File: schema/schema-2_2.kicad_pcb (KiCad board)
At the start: 2 copper layers, 91.4 x 55.9 mm, 16 parts, among them J1 Conn_01x04_Male, J2 Conn_01x04_Male, J3 Conn_01x05_Male

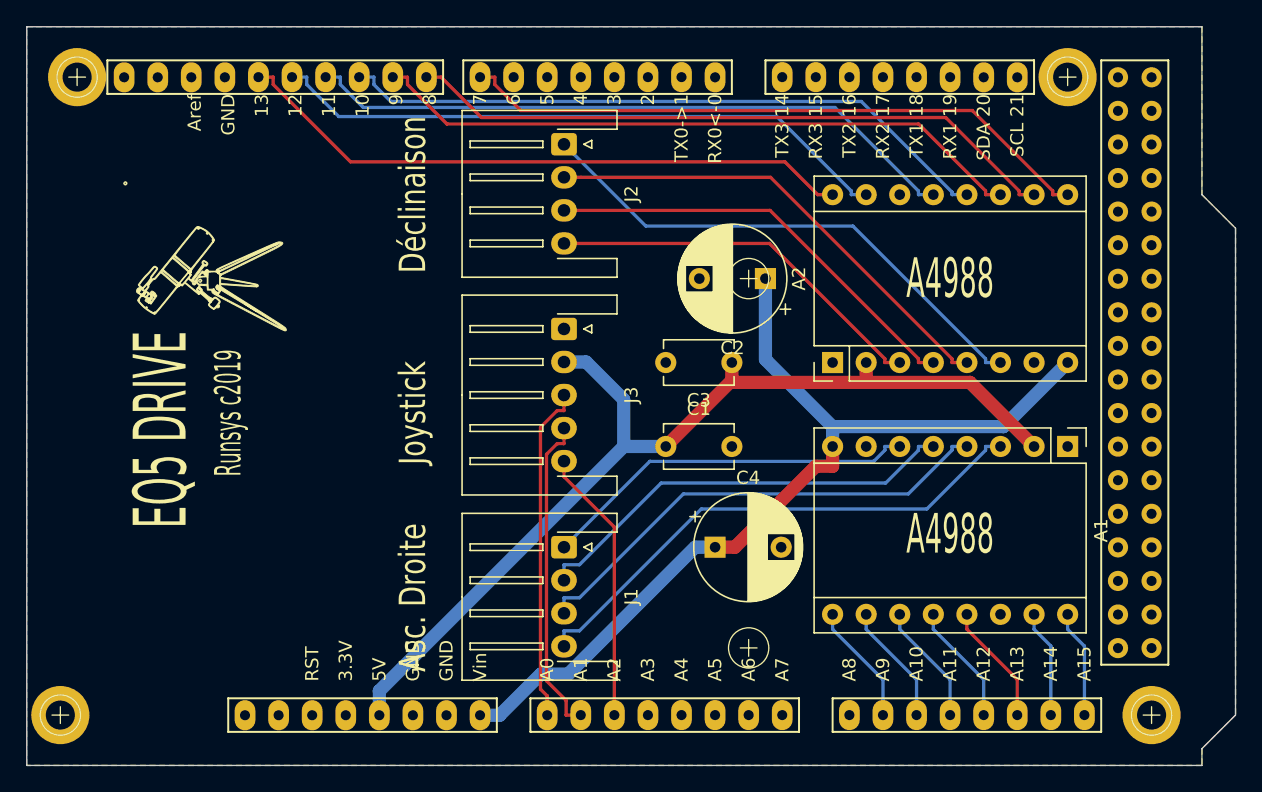
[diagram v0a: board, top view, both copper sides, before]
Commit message: Changement des noms de version Ajout de la macro python freeroute.py
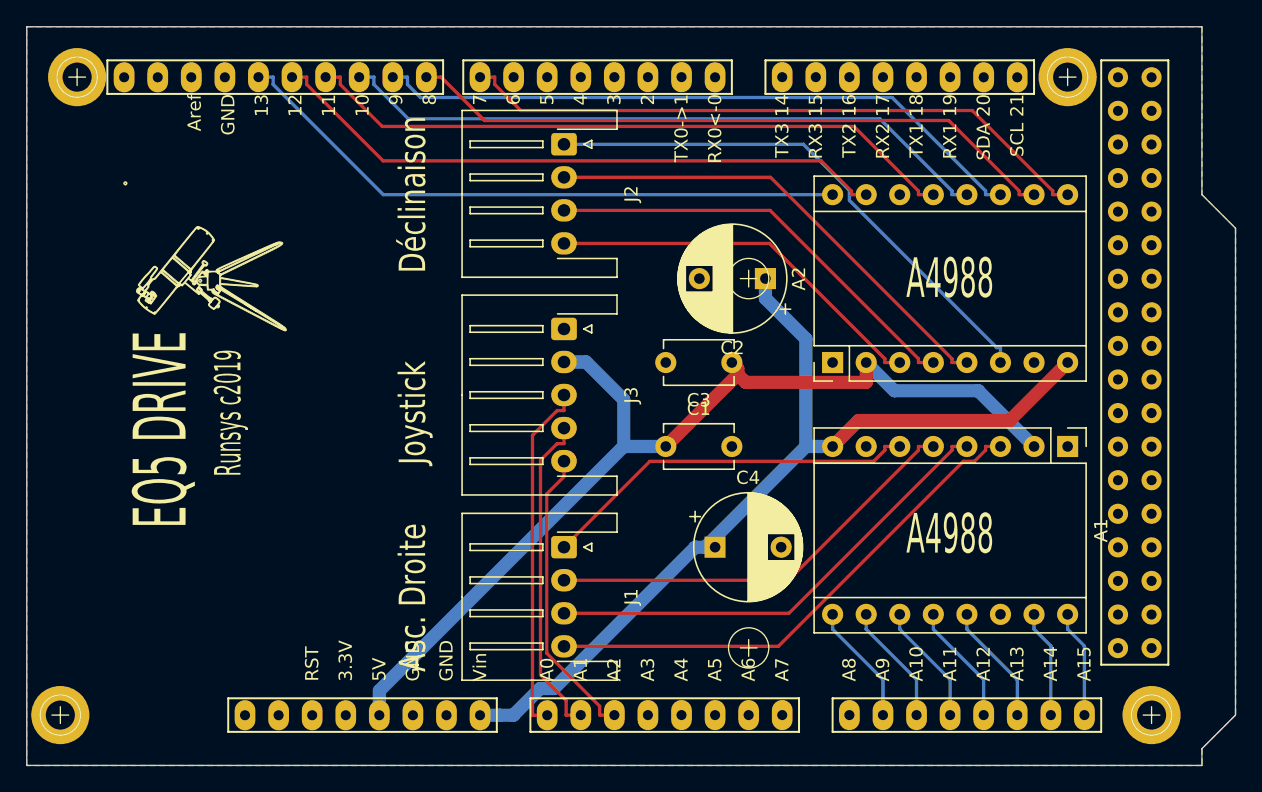
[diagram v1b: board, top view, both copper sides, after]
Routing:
- net /A2: track 20.8 -> 22.5 mm
- net /A0: track 25.5 -> 26.6 mm
- net Net-(A2-Pad6): track 40.0 -> 41.0 mm
- net +5V: track 75.3 -> 76.0 mm
- net Net-(A1-Pad5): track 33.0 -> 32.3 mm
- net Net-(A1-Pad4): track 36.6 -> 35.9 mm
- net Net-(A1-Pad3): track 40.1 -> 39.4 mm
